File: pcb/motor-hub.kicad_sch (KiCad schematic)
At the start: 3 parts, among them U1 STM32G431CBUx, U2 74HC595, U3 74HC595

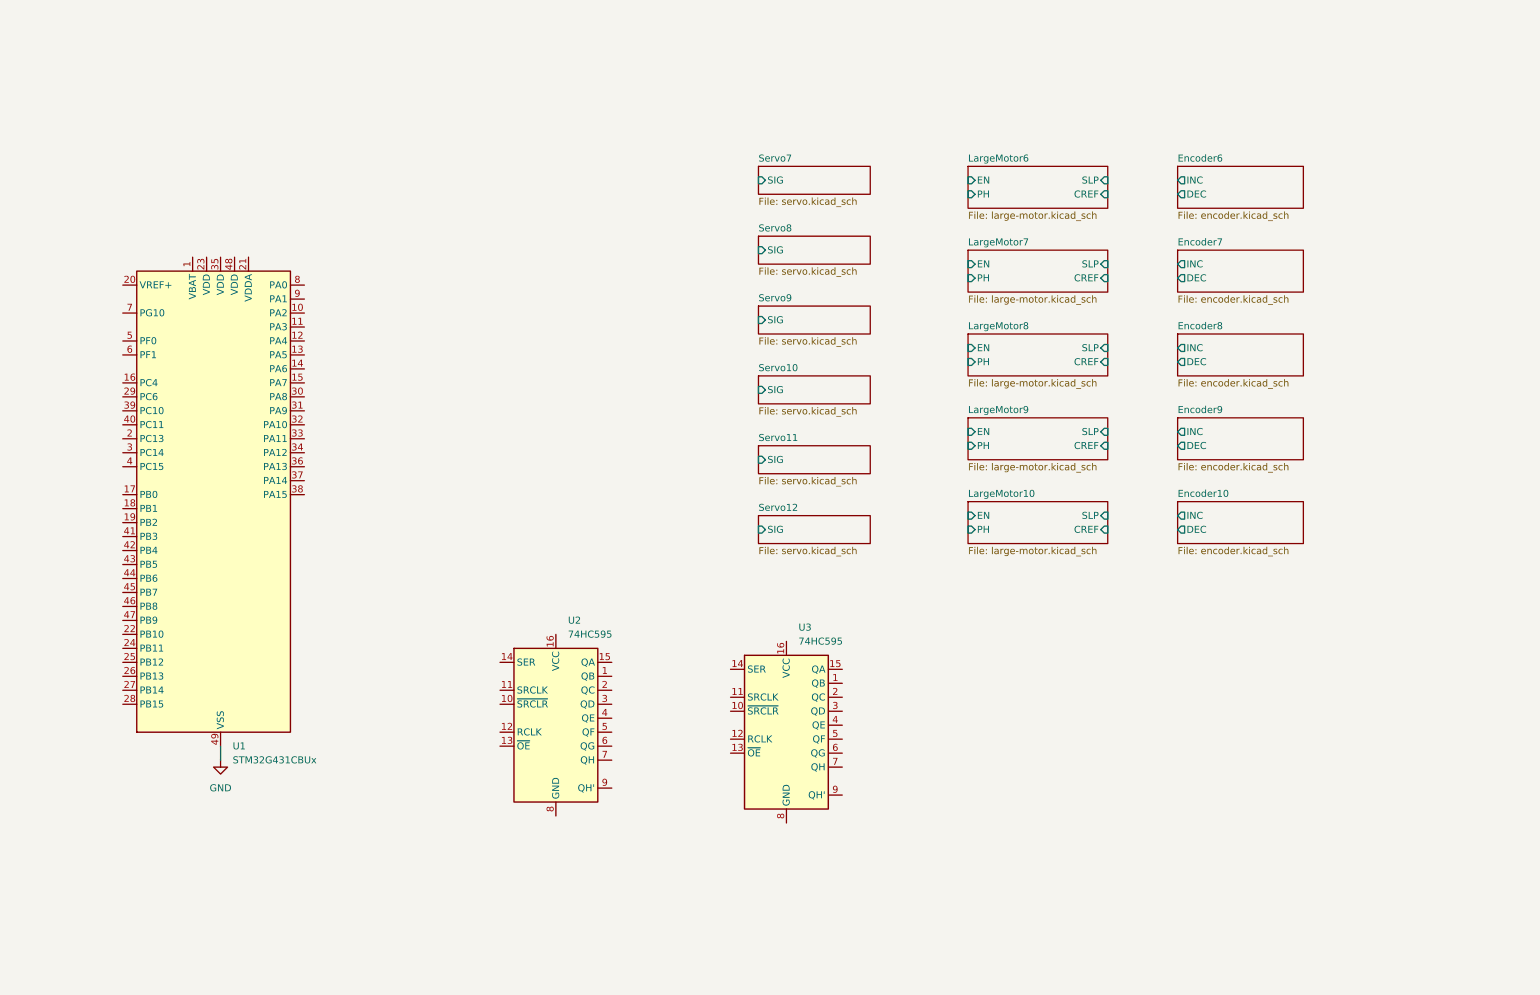
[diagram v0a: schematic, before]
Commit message: Remove sensor hub
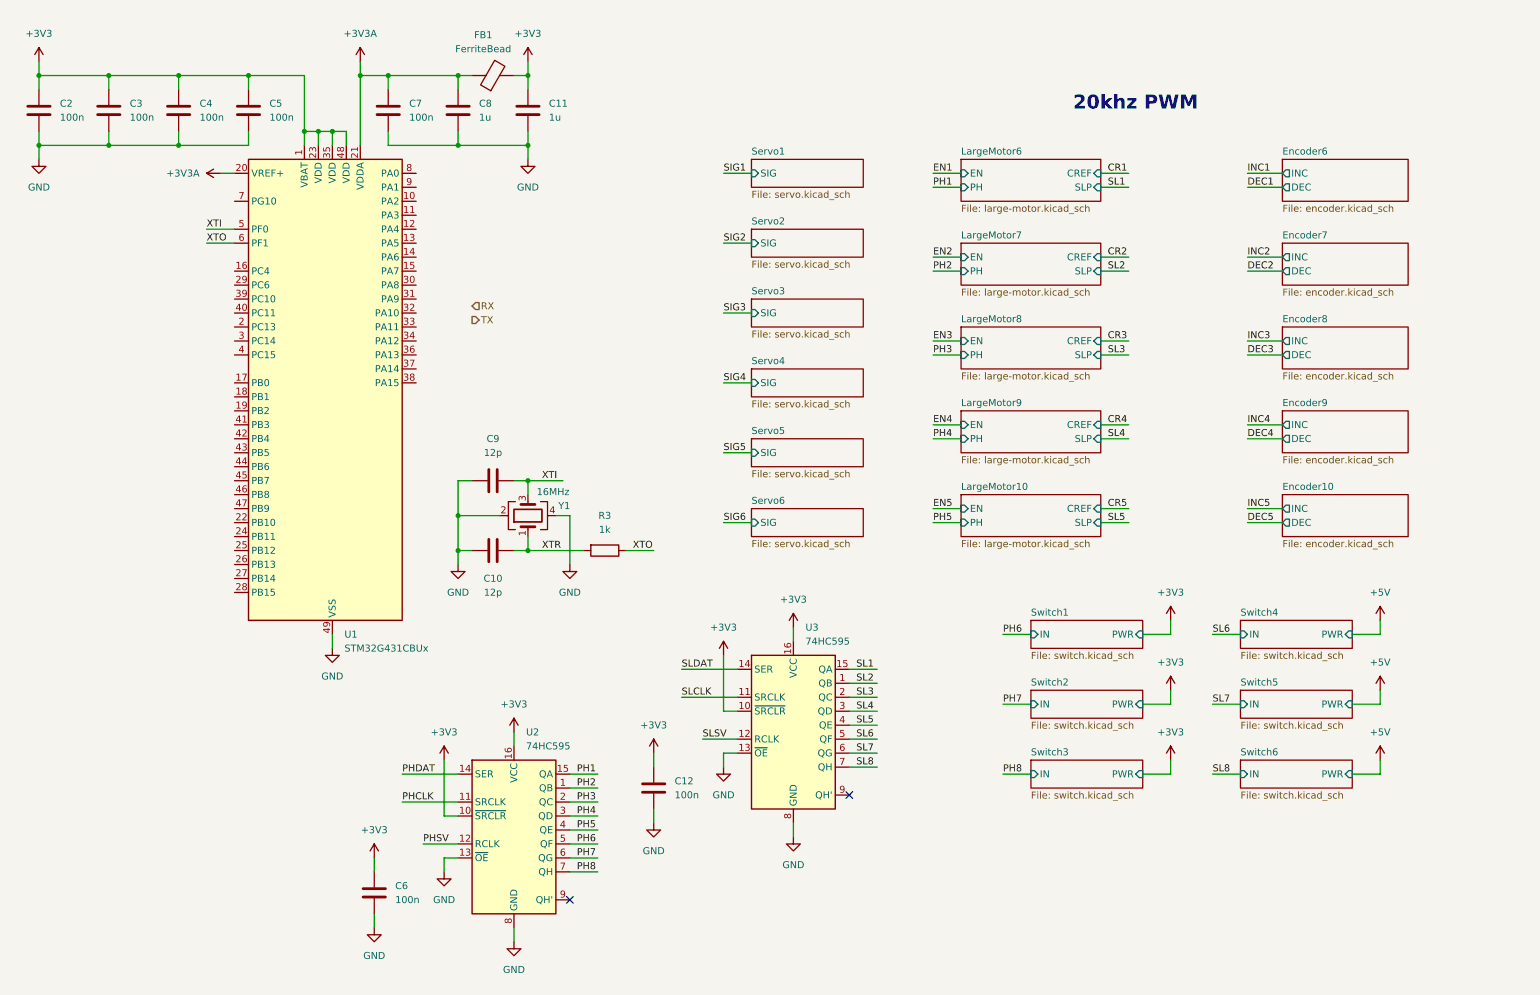
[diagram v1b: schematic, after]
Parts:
- added C10, C9: 12p, Capacitor_SMD:C_0402_1005Metric, symbol Device:C
- added C11, C8: 1u, Capacitor_SMD:C_0402_1005Metric, symbol Device:C
- added C12, C2, C3, C4, C5, C6, C7: 100n, Capacitor_SMD:C_0402_1005Metric, symbol Device:C
- added FB1: FerriteBead, Inductor_SMD:L_0805_2012Metric, symbol Device:FerriteBead
- added R3: 1k, Resistor_SMD:R_0402_1005Metric, symbol Device:R
- added Y1: 16MHz, Crystal:Crystal_SMD_3225-4Pin_3.2x2.5mm, symbol Device:Crystal_GND24
- U1: LCSC (none) -> C529356
- U2, U3: footprint (none) -> Package_SO:SOIC-16_3.9x9.9mm_P1.27mm; LCSC (none) -> C110383
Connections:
- net GND: now also U2.13 (~{OE}), U2.8 (GND), U3.13 (~{OE}), U3.8 (GND), C10.1, C11.2, C12.2, C2.2, C3.2, C4.2, C5.2, C6.2, C7.2, C8.2, C9.1, Y1.2, Y1.4
- net +3V3: now reaches U1.1 (VBAT)
- net +3V3: now also U1.23 (VDD), U1.35 (VDD), U1.48 (VDD), U2.10 (~{SRCLR}), U2.16 (VCC), U3.10 (~{SRCLR}), U3.16 (VCC), C11.1, C12.1, C2.1, C3.1, C4.1, C5.1, C6.1, FB1.2
- net +3V3A: now reaches U1.20 (VREF+)
- net +3V3A: now also U1.21 (VDDA), C7.1, C8.1, FB1.1
- net XTI: now reaches U1.5 (PF0)
- net XTI: now also C9.2, Y1.3
- net XTO: now reaches U1.6 (PF1)
- net XTO: now also R3.1
- net PH2: now reaches U2.1 (QB)
- net PHCLK: now reaches U2.11 (SRCLK)
- net PHSV: now reaches U2.12 (RCLK)
- net PHDAT: now reaches U2.14 (SER)
- net PH1: now reaches U2.15 (QA)
- net PH3: now reaches U2.2 (QC)
- net PH4: now reaches U2.3 (QD)
- net PH5: now reaches U2.4 (QE)
- net PH6: now reaches U2.5 (QF)
- net PH7: now reaches U2.6 (QG)
- net PH8: now reaches U2.7 (QH)
- net SL2: now reaches U3.1 (QB)
- net SLCLK: now reaches U3.11 (SRCLK)
- net SLSV: now reaches U3.12 (RCLK)
- net SLDAT: now reaches U3.14 (SER)
- net SL1: now reaches U3.15 (QA)
- net SL3: now reaches U3.2 (QC)
- net SL4: now reaches U3.3 (QD)
- net SL5: now reaches U3.4 (QE)
- net SL6: now reaches U3.5 (QF)
- net SL7: now reaches U3.6 (QG)
- net SL8: now reaches U3.7 (QH)
- new net XTR: C10.2, R3.2, Y1.1
- no-connect marks 0 -> 2
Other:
- sheet Servo10 renamed Servo4
- sheet Servo11 renamed Servo5
- sheet Servo12 renamed Servo6
- sheet Servo7 renamed Servo1
- sheet Servo8 renamed Servo2
- sheet Servo9 renamed Servo3
- added sheet Switch1 (switch.kicad_sch)
- added sheet Switch2 (switch.kicad_sch)
- added sheet Switch3 (switch.kicad_sch)
- added sheet Switch4 (switch.kicad_sch)
- added sheet Switch5 (switch.kicad_sch)
- added sheet Switch6 (switch.kicad_sch)
- note added: "20khz PWM"
- moved on the sheet: U1, U3

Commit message: Finish schematic
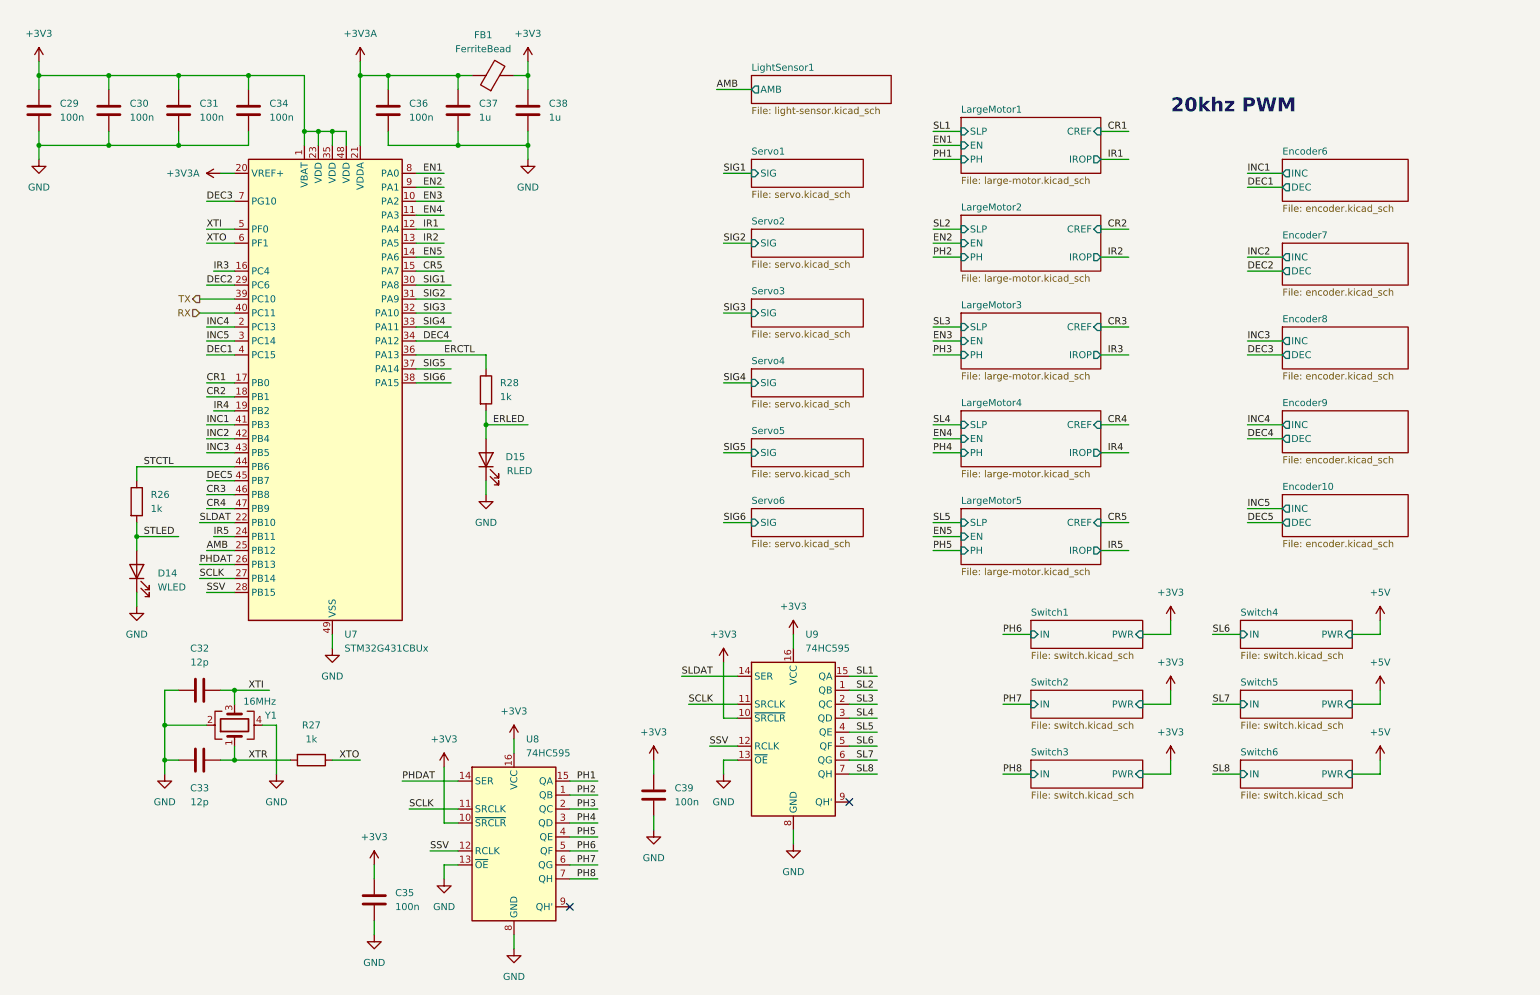
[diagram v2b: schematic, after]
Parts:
- added D14: WLED, LED_SMD:LED_0603_1608Metric, symbol Device:LED
- added D15: RLED, LED_SMD:LED_0603_1608Metric, symbol Device:LED
- added R26, R28: 1k, Resistor_SMD:R_0402_1005Metric, symbol Device:R
- renumbered C2 to C29, C3 to C30, C4 to C31, C9 to C32, C10 to C33, C5 to C34, C6 to C35, C7 to C36, C8 to C37, C11 to C38, C12 to C39, R3 to R27, U1 to U7, U2 to U8, U3 to U9
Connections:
- net PHCLK is gone; now on net SCLK: U8.11 (SRCLK)
- net PHSV is gone; now on net SSV: U8.12 (RCLK)
- net SLCLK is gone; now on net SCLK: U9.11 (SRCLK)
- net SLSV is gone; now on net SSV: U9.12 (RCLK)
- net CR1: now also U7.17 (PB0)
- net CR2: now also U7.18 (PB1)
- net CR3: now also U7.46 (PB8)
- net CR4: now also U7.47 (PB9)
- net CR5: now also U7.15 (PA7)
- net DEC1: now also U7.4 (PC15)
- net DEC2: now also U7.29 (PC6)
- net DEC3: now also U7.7 (PG10)
- net DEC4: now also U7.34 (PA12)
- net DEC5: now also U7.45 (PB7)
- net EN1: now also U7.8 (PA0)
- net EN2: now also U7.9 (PA1)
- net EN3: now also U7.10 (PA2)
- net EN4: now also U7.11 (PA3)
- net EN5: now also U7.14 (PA6)
- net GND: now also D14.1 (K), D15.1 (K)
- net INC1: now also U7.41 (PB3)
- net INC2: now also U7.42 (PB4)
- net INC3: now also U7.43 (PB5)
- net INC4: now also U7.2 (PC13)
- net INC5: now also U7.3 (PC14)
- net PHDAT: now also U7.26 (PB13)
- net RX: now also U7.40 (PC11)
- net SIG1: now also U7.30 (PA8)
- net SIG2: now also U7.31 (PA9)
- net SIG3: now also U7.32 (PA10)
- net SIG4: now also U7.33 (PA11)
- net SIG5: now also U7.37 (PA14)
- net SIG6: now also U7.38 (PA15)
- net SLDAT: now also U7.22 (PB10)
- net TX: now also U7.39 (PC10)
- net IR1: now reaches U7.12 (PA4)
- net IR2: now reaches U7.13 (PA5)
- net IR3: now reaches U7.16 (PC4)
- net IR4: now reaches U7.19 (PB2)
- net IR5: now reaches U7.24 (PB11)
- net AMB: now reaches U7.25 (PB12)
- net SCLK: now reaches U7.27 (PB14)
- net SSV: now reaches U7.28 (PB15)
- net ERCTL: now reaches U7.36 (PA13)
- net ERCTL: now also R28.1
- net STCTL: now reaches U7.44 (PB6)
- net STCTL: now also R26.1
- new net ERLED: D15.2 (A), R28.2
- new net STLED: D14.2 (A), R26.2
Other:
- sheet LargeMotor6 renamed LargeMotor1
- removed sheet LargeMotor10
- removed sheet LargeMotor7
- removed sheet LargeMotor8
- removed sheet LargeMotor9
- added sheet LargeMotor2 (large-motor.kicad_sch)
- added sheet LargeMotor3 (large-motor.kicad_sch)
- added sheet LargeMotor4 (large-motor.kicad_sch)
- added sheet LargeMotor5 (large-motor.kicad_sch)
- added sheet LightSensor1 (light-sensor.kicad_sch)
- sheet LargeMotor1 ports: added IROP; removed none
- moved on the sheet: C32, C33, C35, C39, R27, U8, U9, Y1

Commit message: Save progress
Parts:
- removed C39: 100n, Capacitor_SMD:C_0402_1005Metric, symbol Device:C
- removed D14: WLED, LED_SMD:LED_0603_1608Metric, symbol Device:LED
- removed D15: RLED, LED_SMD:LED_0603_1608Metric, symbol Device:LED
- removed R26: 1k, Resistor_SMD:R_0402_1005Metric, symbol Device:R
- removed U9: 74HC595, Package_SO:SOIC-16_3.9x9.9mm_P1.27mm, symbol 74xx:74HC595
- added C1, C13: 100u, Capacitor_SMD:C_Elec_8x6.2, symbol Device:C
- added D16: WLED, LED_SMD:LED_0603_1608Metric, symbol Device:LED
- added J11: Screw_Terminal_01x10, TerminalBlock_Phoenix:TerminalBlock_Phoenix_MKDS-1,5-10_1x10_P5.00mm_Horizontal, symbol Connector:Screw_Terminal_01x10
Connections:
- net PH6 is gone; now on net SL3: U8.5 (QF)
- net PH7 is gone; now on net PH4: U8.6 (QG)
- net PH8 is gone; now on net SL4: U8.7 (QH)
- net SLDAT is gone; now on net PH5: U7.22 (PB10)
- net STCTL is gone; now on net SL5: U7.44 (PB6)
- net GND: now also C1.2, C13.2, D16.1 (K)
- net PH2: now also U8.2 (QC); no longer U8.1 (QB)
- net PH3: now also U8.4 (QE); no longer U8.2 (QC)
- net PH4: no longer U8.3 (QD)
- net PH5: no longer U8.4 (QE)
- net SL1: now also U8.1 (QB)
- net SL2: now also U8.3 (QD)
- net ERCTL renamed SCTL
- net ERLED renamed SLED
- net SLED: now also D16.2 (A)
- net PHDAT renamed RDAT
- net SCLK renamed RCLK
- net SSV renamed RSV
- new net OA1: J11.1 (Pin_1)
- new net OA2: J11.3 (Pin_3)
- new net OA3: J11.5 (Pin_5)
- new net OA4: J11.7 (Pin_7)
- new net OA5: J11.9 (Pin_9)
- new net OB1: J11.2 (Pin_2)
- new net OB2: J11.4 (Pin_4)
- new net OB3: J11.6 (Pin_6)
- new net OB4: J11.8 (Pin_8)
- new net OB5: J11.10 (Pin_10)
- new net VDD: C1.1, C13.1
- no-connect marks 2 -> 1
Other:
- sheet Encoder10 renamed Encoder5
- sheet Encoder6 renamed Encoder1
- sheet Encoder7 renamed Encoder2
- sheet Encoder8 renamed Encoder3
- sheet Encoder9 renamed Encoder4
- removed sheet Switch1
- removed sheet Switch2
- removed sheet Switch3
- removed sheet Switch4
- removed sheet Switch5
- removed sheet Switch6
- sheet LargeMotor1 ports: added OUTA, OUTB; removed none
- sheet LargeMotor2 ports: added OUTA, OUTB; removed none
- sheet LargeMotor3 ports: added OUTA, OUTB; removed none
- sheet LargeMotor4 ports: added OUTA, OUTB; removed none
- sheet LargeMotor5 ports: added OUTA, OUTB; removed none
